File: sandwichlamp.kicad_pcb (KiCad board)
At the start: 2 copper layers, 96 x 96 mm, 27 parts, among them J1 Pole1, J2 Pole2, J3 Pole3, J4 12V Enable, J5 HLK-LD2410C, J6 Conn_01x02, J7 Conn_01x03, SW1 Rader Power, SW3 POWER, U1 magnetic-charger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

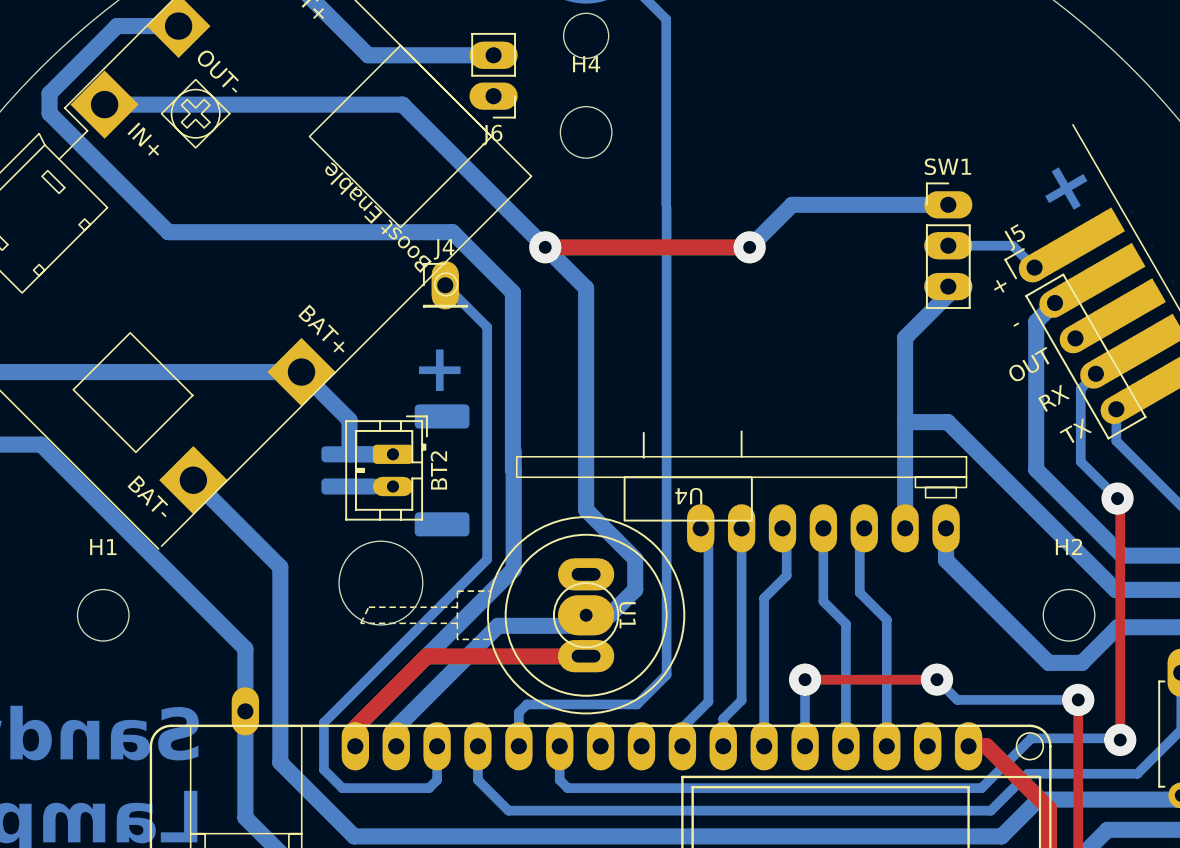
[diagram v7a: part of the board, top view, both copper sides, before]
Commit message: Cleanup schematic and pcb
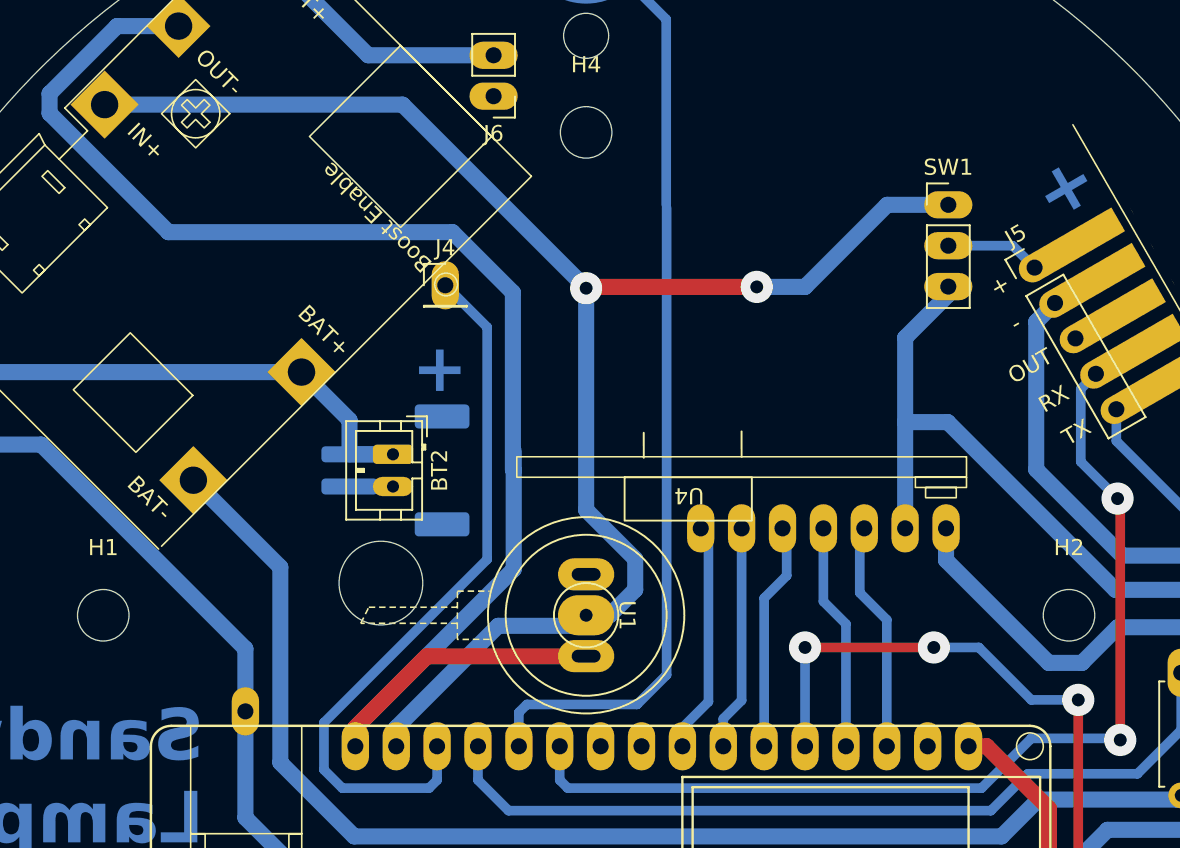
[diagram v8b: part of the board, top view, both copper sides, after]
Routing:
- net Touch2: track 46.5 -> 49.3 mm
- net +5V: track 100.3 -> 98.8 mm
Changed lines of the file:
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@@
 	)
 	(segment
-		(start 110.16 77.14)
-		(end 97.46 77.14)
+		(start 110.6 79.6)
+		(end 100.08 79.6)
+		(width 1)
+		(layer "F.Cu")
+		(net 1)
+	)
+	(segment
+		(start 100.08 79.6)
+		(end 100 79.68)
 		(width 1)
 		(layer "F.Cu")
@@
 	)
 	(via
-		(at 97.46 77.14)
+		(at 100 79.68)
 		(size 2)
 		(drill 0.8)
@@
 	)
 	(via
-		(at 110.16 77.14)
+		(at 110.6 79.6)
 		(size 2)
 		(drill 0.8)
@@
 	)
 	(segment
+		(start 100 93.457308)
+		(end 103.050001 96.507309)
+		(width 1)
+		(layer "B.Cu")
+		(net 1)
+	)
+	(segment
 		(start 94.533746 100.655695)
 		(end 99.344305 100.655695)
@@
 	)
 	(segment
+		(start 101.462692 100)
+		(end 100 100)
+		(width 1)
+		(layer "B.Cu")
+		(net 1)
+	)
+	(segment
 		(start 88.594858 68.274858)
-		(end 97.46 77.14)
-		(width 1)
-		(layer "B.Cu")
-		(net 1)
-	)
-	(segment
-		(start 70.084263 68.274858)
+		(end 70.084263 68.274858)
+		(width 1)
+		(layer "B.Cu")
+		(net 1)
+	)
+	(segment
+		(start 113.6 79.6)
+		(end 118.7 74.5)
+		(width 1)
+		(layer "B.Cu")
+		(net 1)
+	)
+	(segment
+		(start 100 79.68)
 		(end 88.594858 68.274858)
 		(width 1)
@@
 	)
 	(segment
-		(start 97.46 77.14)
-		(end 100 79.68)
+		(start 88.2 106.989441)
+		(end 94.533746 100.655695)
+		(width 1)
+		(layer "B.Cu")
+		(net 1)
+	)
+	(segment
+		(start 99.344305 100.655695)
+		(end 100 100)
 		(width 1)
 		(layer "B.Cu")
@@
 	)
 	(segment
-		(start 88.2 106.989441)
-		(end 94.533746 100.655695)
-		(width 1)
-		(layer "B.Cu")
-		(net 1)
-	)
-	(segment
-		(start 100 93.457308)
-		(end 103.050001 96.507309)
-		(width 1)
-		(layer "B.Cu")
-		(net 1)
-	)
-	(segment
-		(start 99.344305 100.655695)
-		(end 100 100)
+		(start 118.7 74.5)
+		(end 122.5 74.5)
 		(width 1)
 		(layer "B.Cu")
@@
 	)
 	(segment
-		(start 101.462692 100)
-		(end 100 100)
-		(width 1)
-		(layer "B.Cu")
-		(net 1)
-	)
-	(segment
-		(start 122.5 74.5)
-		(end 112.8 74.5)
+		(start 110.6 79.6)
+		(end 113.6 79.6)
 		(width 1)
 		(layer "B.Cu")
@@
 		(start 103.050001 98.412691)
 		(end 101.462692 100)
-		(width 1)
-		(layer "B.Cu")
-		(net 1)
-	)
-	(segment
-		(start 112.8 74.5)
-		(end 110.16 77.14)
 		(width 1)
 		(layer "B.Cu")
@@
 	)
 	(segment
+		(start 121.6 102)
+		(end 113.6 102)
+		(width 0.6)
+		(layer "F.Cu")
+		(net 21)
+	)
+	(segment
 		(start 130.57502 105.258676)
 		(end 130.57502 122.92502)
-		(width 0.6)
-		(layer "F.Cu")
-		(net 21)
-	)
-	(segment
-		(start 113.6 104)
-		(end 121.8 104)
 		(width 0.6)
 		(layer "F.Cu")
@@
 	)
 	(via
-		(at 113.6 104)
+		(at 113.6 102)
 		(size 2)
 		(drill 0.8)
@@
 	)
 	(via
-		(at 121.8 104)
+		(at 121.6 102)
 		(size 2)
 		(drill 0.8)
@@
 	)
 	(segment
-		(start 123.058676 105.258676)
+		(start 127.658676 105.258676)
 		(end 130.57502 105.258676)
 		(width 0.6)
@@
 	)
 	(segment
+		(start 124.4 102)
+		(end 127.658676 105.258676)
+		(width 0.6)
+		(layer "B.Cu")
+		(net 21)
+	)
+	(segment
+		(start 121.6 102)
+		(end 124.4 102)
+		(width 0.6)
+		(layer "B.Cu")
+		(net 21)
+	)
+	(segment
 		(start 113.6 108.14)
-		(end 113.6 104)
-		(width 0.6)
-		(layer "B.Cu")
-		(net 21)
-	)
-	(segment
-		(start 121.8 104)
-		(end 123.058676 105.258676)
-		(width 0.6)
-		(layer "B.Cu")
+		(end 113.6 102)
+		(width 0.6)
+		(layer "B.Cu")
